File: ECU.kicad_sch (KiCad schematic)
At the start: 119 parts, among them J1 Solenoid 0, J10 Thermocouple 3, J13 External SPI, J14 External UART, J15 External I2C, J16 Pressure Transducer 0, J17 Pressure Transducer 1, J18 Pressure Transducer 2, J19 Pressure Transducer 3, J2 Solenoid 1, J20 Pressure Transducer 4, J21 Pressure Transducer 5, J22 Power In, J3 Solenoid 2, J4 Solenoid 3, J5 Solenoid 4, J6 Solenoid 5, J7 Thermocouple 0, J8 Thermocouple 1, J9 Thermocouple 2, U1 Teensy4.1, U10 MAX31855, U11 MAX31855, U12 OPA357, U13 OPA357, U14 OPA357, U15 OPA357, U16 OPA357, U17 OPA357, U2 OPA357, U20 uA7805, U21 TLV2217, U3 OPA357, U4 OPA357, U5 OPA357, U6 OPA357, U7 OPA357, U8 MAX31855, U9 MAX31855

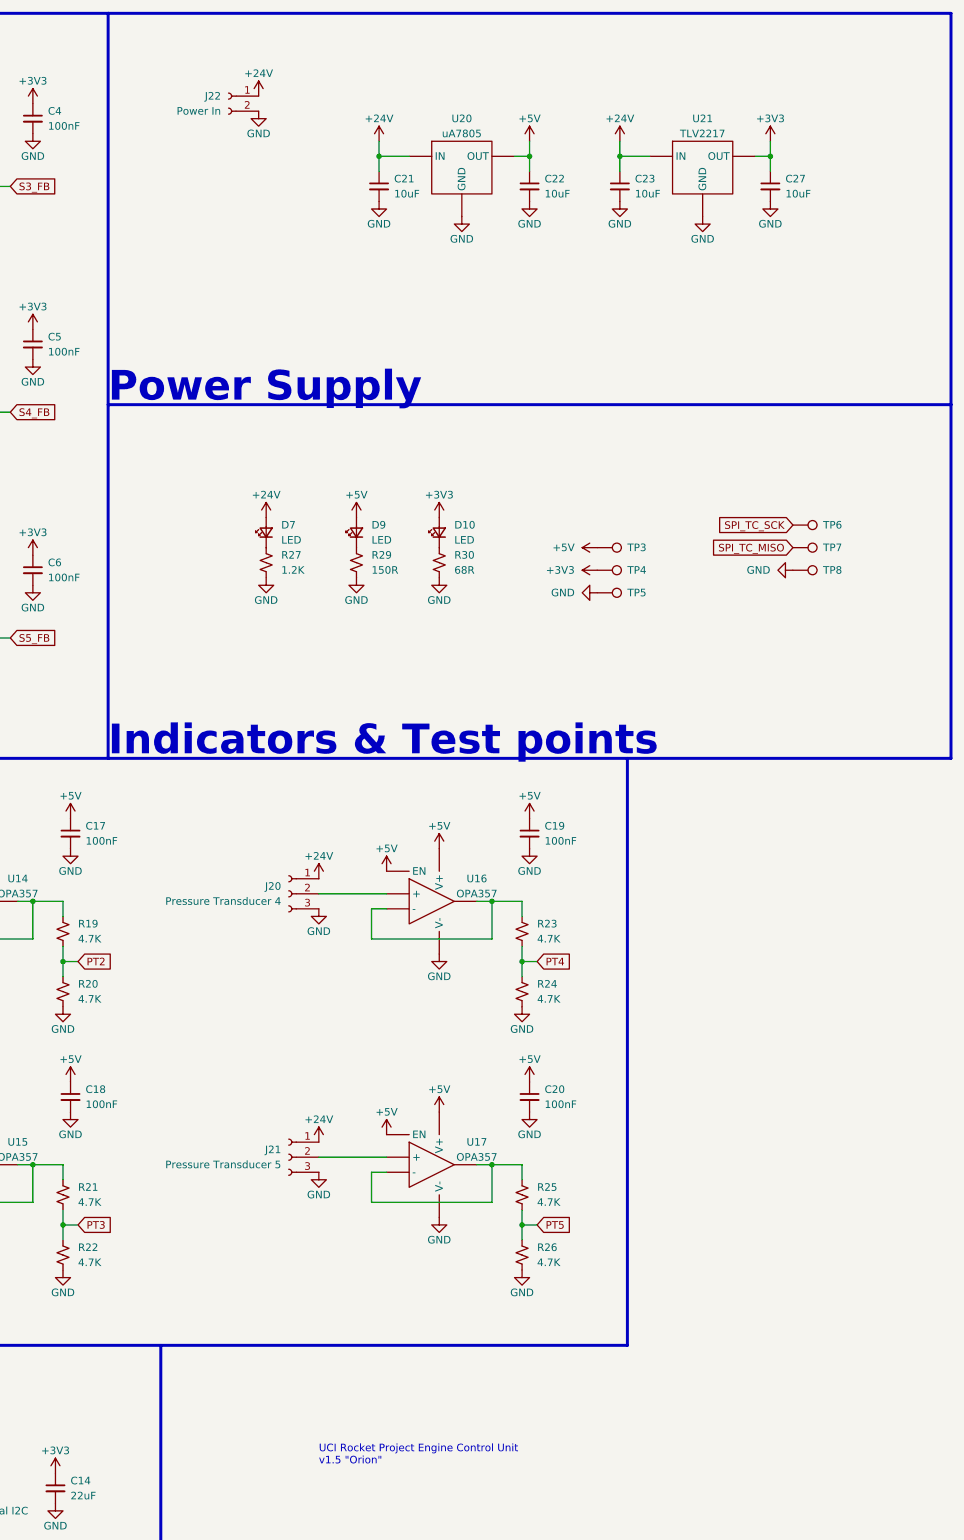
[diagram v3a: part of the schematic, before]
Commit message: Integrate power switching & cutoff system
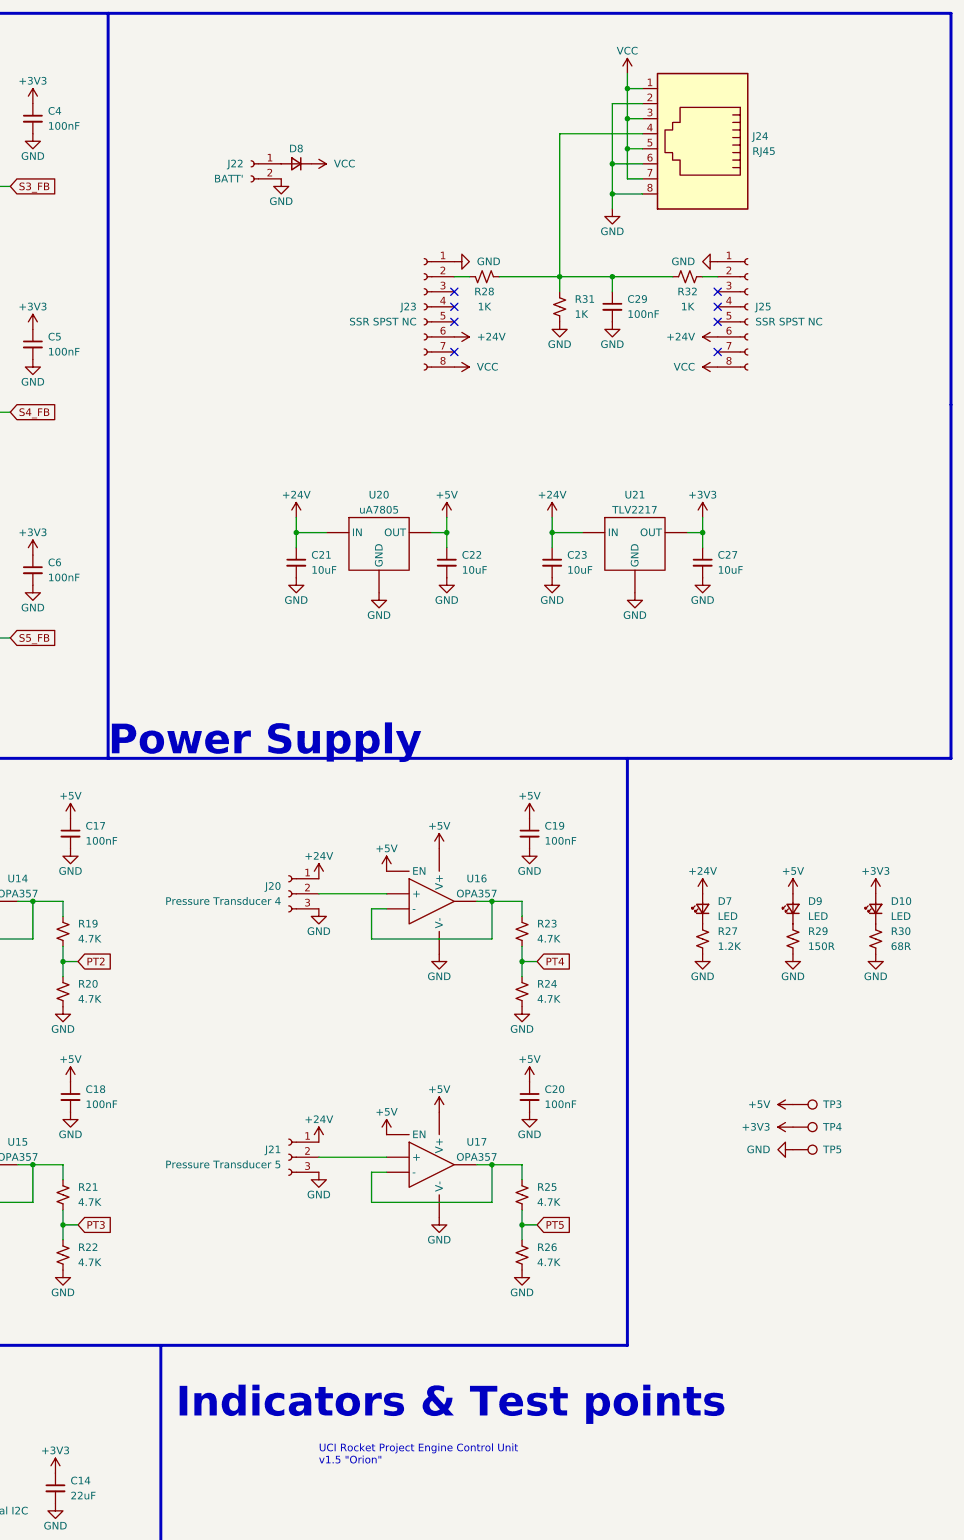
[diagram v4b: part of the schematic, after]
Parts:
- removed TP6, TP7, TP8: ~, TestPoint:TestPoint_Pad_D4.0mm, symbol Connector:TestPoint
- added C29: 100nF, Capacitor_SMD:C_0603_1608Metric, symbol Device:C_Small
- added D8: ~, Diode_SMD:D_SMA, symbol Device:D_Small
- added J23, J25: SSR SPST NC, Package_SIP:SIP-8_19x3mm_P2.54mm, symbol Connector:Conn_01x08_Female
- added J24: RJ45, Connector_RJ:RJ45_Amphenol_54602-x08_Horizontal, symbol Connector:RJ45
- added R28, R31, R32: 1K, Resistor_SMD:R_2512_6332Metric, symbol Device:R_Small_US
- J22: value Power In -> BATT'
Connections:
- net +24V: now also J23.6 (Pin_6), J25.6 (Pin_6); no longer J22.1 (Pin_1)
- net GND: now also C29.2, J23.1 (Pin_1), J24.2, J24.6, J24.8, J25.1 (Pin_1), R31.2
- new net: C29.1, J24.4, R28.1, R31.1, R32.1
- new net: J25.2 (Pin_2), R32.2
- new net: J23.2 (Pin_2), R28.2
- new net: D8.2 (A), J22.1 (Pin_1)
- new net VCC: D8.1 (K), J23.8 (Pin_8), J24.1, J24.3, J24.5, J24.7, J25.8 (Pin_8)
- no-connect marks 26 -> 34
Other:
- moved on the sheet: C21, C22, C23, C27, D10, D7, D9, J22, R27, R29, R30, TP3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
